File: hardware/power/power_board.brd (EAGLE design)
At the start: 92 x 92 mm, 61 parts, among them IC1 LM321MF, IC2 LM321MF, J1 FASTON1289_ST, J2 FASTON1289_ST, J3 12v, J4 5v, J5 XT30PW-F, J6 XT30PW-F, J7 XT30PW-F, J8 XT30PW-F, U1 PDQ30-Q24-S5-D, U2 PDQ30-Q24-S12-D

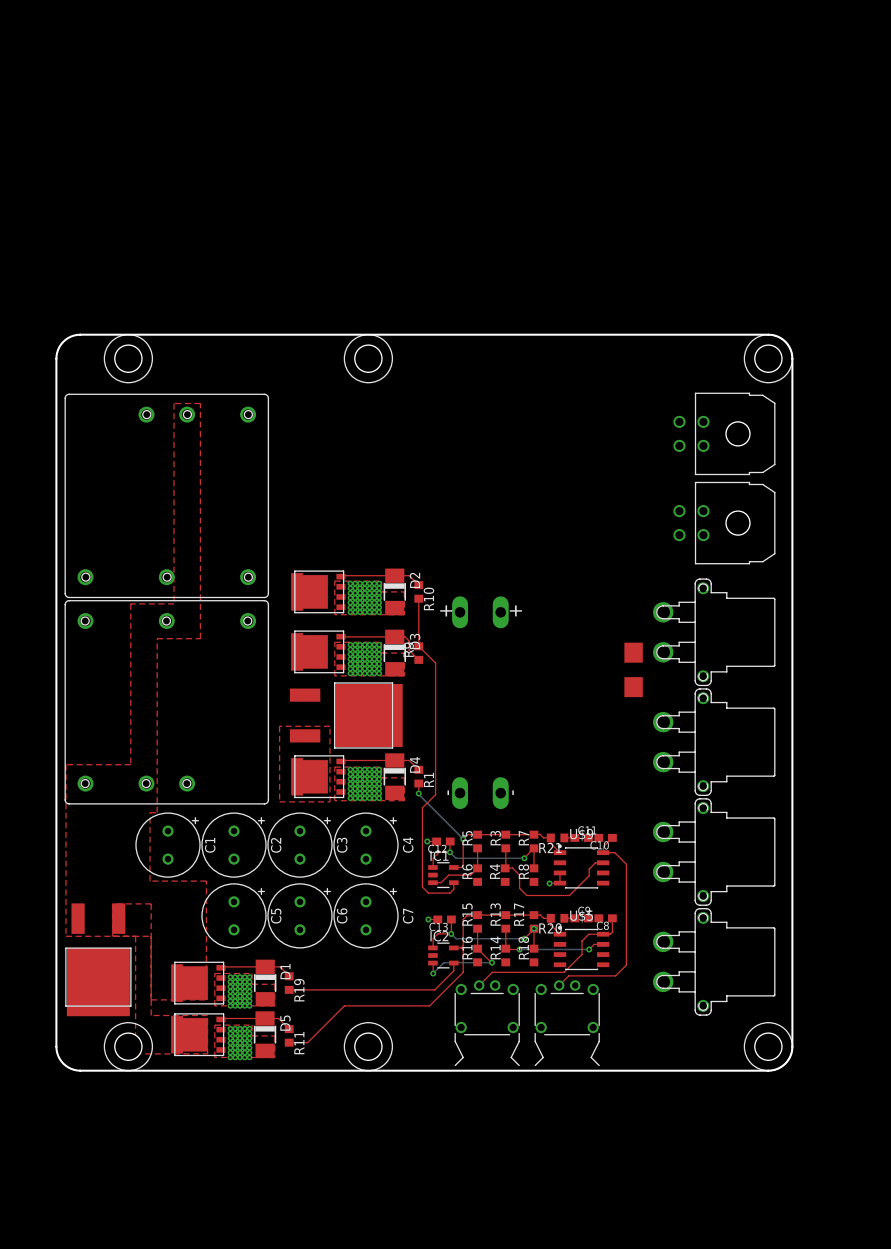
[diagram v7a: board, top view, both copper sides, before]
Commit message: First power plane layout attempt
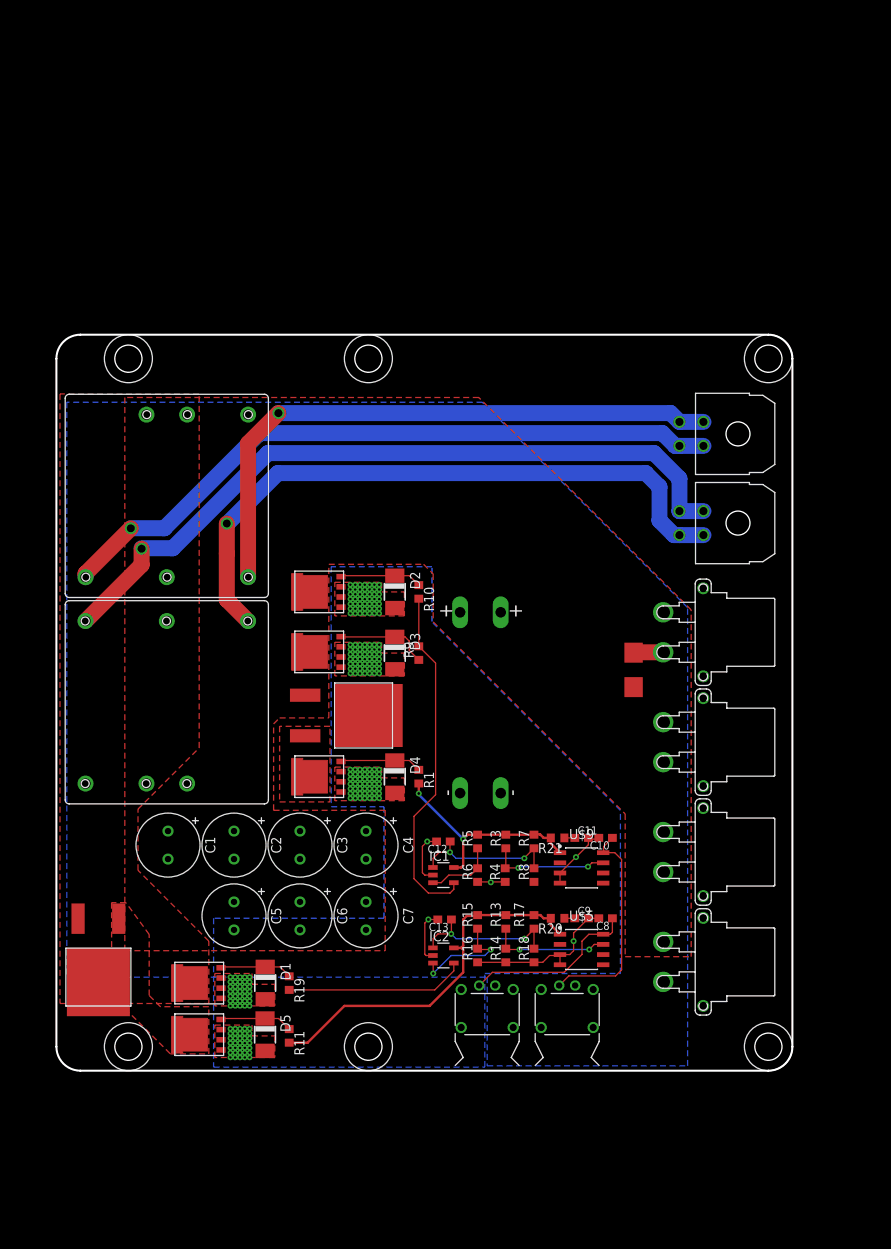
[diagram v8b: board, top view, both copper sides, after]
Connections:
- net +24V renamed BATT_+24V
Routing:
- net 5V_GND: track 0.00 -> 92.5 mm, vias 0 -> 1
- net +12VOUT: track 0.00 -> 85.6 mm, vias 0 -> 1
- net +5VOUT: track 0.00 -> 81.1 mm, vias 0 -> 1
- net 12V_GND: track 0.00 -> 75.7 mm, vias 0 -> 1
- net BATT_GND: track 4.96 -> 45.5 mm, vias 220 -> 222
- net N$3: track 19.3 -> 15.1 mm, vias 0 -> 2
- net BATT_+24V: track 0.00 -> 3.72 mm
- net N$6: track 42.9 -> 43.7 mm
- net N$13: vias 3 -> 2
- added copper zone on layer 16, net BATT_+24V
- added copper zone on layer 16, net BATT_GND
- added copper zone on layer 1, net LEG_GND
